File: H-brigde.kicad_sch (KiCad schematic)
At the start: 17 parts, among them J1 track out, J2 track out, U1 L298N

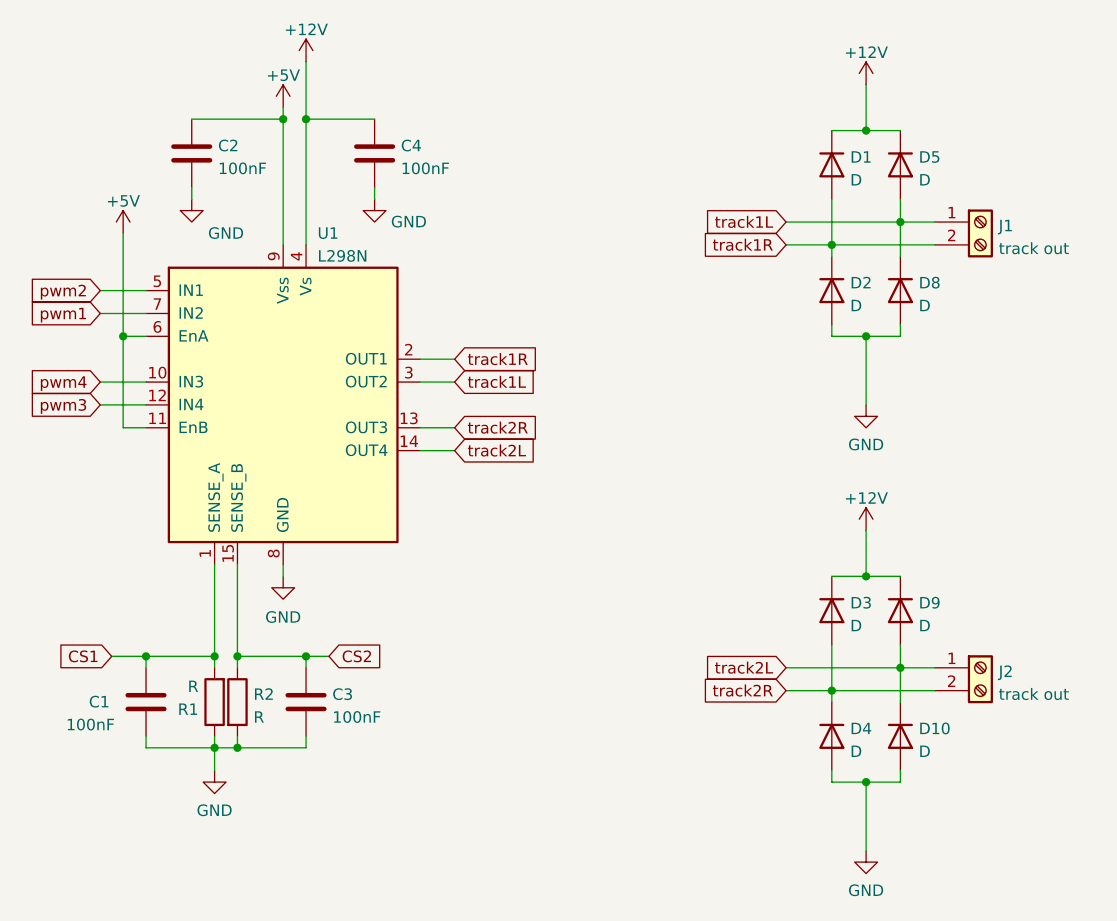
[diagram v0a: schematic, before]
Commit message: redone the switch connectors to accomodate a current sense print. Rearranged parts and updated silk texts to be 50% of their original size
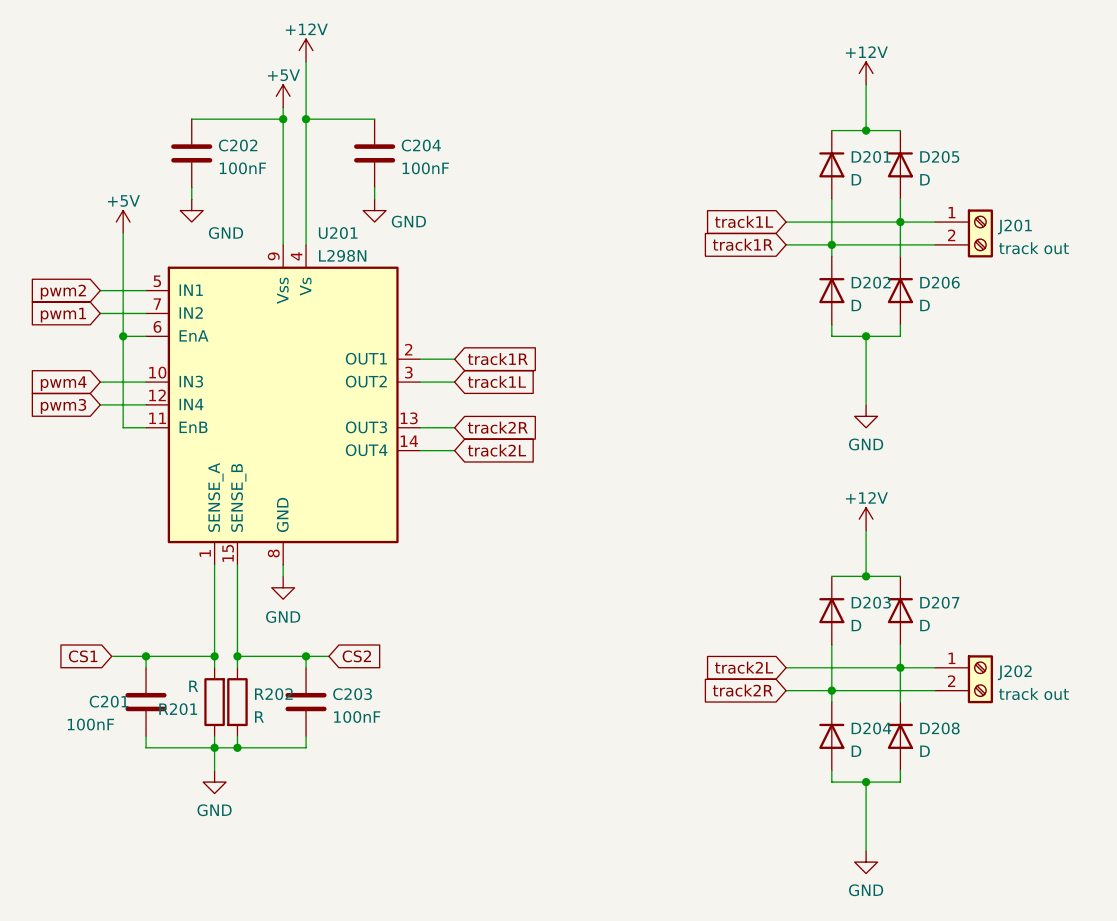
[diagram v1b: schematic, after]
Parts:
- renumbered C1 to C201, C2 to C202, C3 to C203, C4 to C204, D1 to D201, D2 to D202, D3 to D203, D4 to D204, D5 to D205, D8 to D206, D9 to D207, D10 to D208, J1 to J201, J2 to J202, R1 to R201, R2 to R202, U1 to U201
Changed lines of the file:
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@@
   (symbol (lib_id "Device:R") (at 115.57 129.54 180) (unit 1)
     (in_bom yes) (on_board yes) (fields_autoplaced)
-    (property "Reference" "R1" (id 0) (at 113.792 130.3747 0)
+    (property "Reference" "R201" (id 0) (at 113.792 130.3747 0)
       (effects (font (size 1.27 1.27)) (justify left))
     )
@@
   (symbol (lib_id "Device:C") (at 113.03 68.58 0) (unit 1)
     (in_bom yes) (on_board yes) (fields_autoplaced)
-    (property "Reference" "C2" (id 0) (at 115.951 67.7453 0)
+    (property "Reference" "C202" (id 0) (at 115.951 67.7453 0)
       (effects (font (size 1.27 1.27)) (justify left))
     )
@@
   (symbol (lib_id "Device:D") (at 184.15 83.82 270) (unit 1)
     (in_bom yes) (on_board yes) (fields_autoplaced)
-    (property "Reference" "D2" (id 0) (at 186.182 82.9853 90)
+    (property "Reference" "D202" (id 0) (at 186.182 82.9853 90)
       (effects (font (size 1.27 1.27)) (justify left))
     )
@@
   (symbol (lib_id "power:+5V") (at 123.19 63.5 0) (unit 1)
     (in_bom yes) (on_board yes) (fields_autoplaced)
-    (property "Reference" "#PWR0106" (id 0) (at 123.19 67.31 0)
+    (property "Reference" "#PWR0204" (id 0) (at 123.19 67.31 0)
       (effects (font (size 1.27 1.27)) hide)
     )
@@
   (symbol (lib_id "power:+12V") (at 187.96 110.49 0) (unit 1)
     (in_bom yes) (on_board yes) (fields_autoplaced)
-    (property "Reference" "#PWR0103" (id 0) (at 187.96 114.3 0)
+    (property "Reference" "#PWR0210" (id 0) (at 187.96 114.3 0)
       (effects (font (size 1.27 1.27)) hide)
     )
@@
   (symbol (lib_id "power:GND") (at 115.57 137.16 0) (unit 1)
     (in_bom yes) (on_board yes) (fields_autoplaced)
-    (property "Reference" "#PWR0114" (id 0) (at 115.57 143.51 0)
+    (property "Reference" "#PWR0203" (id 0) (at 115.57 143.51 0)
       (effects (font (size 1.27 1.27)) hide)
     )
@@
   (symbol (lib_id "power:GND") (at 187.96 96.52 0) (unit 1)
     (in_bom yes) (on_board yes) (fields_autoplaced)
-    (property "Reference" "#PWR0102" (id 0) (at 187.96 102.87 0)
+    (property "Reference" "#PWR0209" (id 0) (at 187.96 102.87 0)
       (effects (font (size 1.27 1.27)) hide)
     )
@@
   (symbol (lib_id "Device:D") (at 191.77 83.82 270) (unit 1)
     (in_bom yes) (on_board yes) (fields_autoplaced)
-    (property "Reference" "D8" (id 0) (at 193.802 82.9853 90)
+    (property "Reference" "D206" (id 0) (at 193.802 82.9853 90)
       (effects (font (size 1.27 1.27)) (justify left))
     )
@@
   (symbol (lib_id "power:+5V") (at 105.41 77.47 0) (unit 1)
     (in_bom yes) (on_board yes) (fields_autoplaced)
-    (property "Reference" "#PWR0104" (id 0) (at 105.41 81.28 0)
+    (property "Reference" "#PWR0201" (id 0) (at 105.41 81.28 0)
       (effects (font (size 1.27 1.27)) hide)
     )
@@
   (symbol (lib_id "power:GND") (at 133.35 73.66 0) (unit 1)
     (in_bom yes) (on_board yes)
-    (property "Reference" "#PWR0111" (id 0) (at 133.35 80.01 0)
+    (property "Reference" "#PWR0207" (id 0) (at 133.35 80.01 0)
       (effects (font (size 1.27 1.27)) hide)
     )
@@
   (symbol (lib_id "Device:D") (at 184.15 119.38 270) (unit 1)
     (in_bom yes) (on_board yes) (fields_autoplaced)
-    (property "Reference" "D3" (id 0) (at 186.182 118.5453 90)
+    (property "Reference" "D203" (id 0) (at 186.182 118.5453 90)
       (effects (font (size 1.27 1.27)) (justify left))
     )
@@
   (symbol (lib_id "power:+12V") (at 125.73 58.42 0) (unit 1)
     (in_bom yes) (on_board yes) (fields_autoplaced)
-    (property "Reference" "#PWR0110" (id 0) (at 125.73 62.23 0)
+    (property "Reference" "#PWR0206" (id 0) (at 125.73 62.23 0)
       (effects (font (size 1.27 1.27)) hide)
     )
@@
   (symbol (lib_id "Driver_Motor:L298N") (at 123.19 96.52 0) (unit 1)
     (in_bom yes) (on_board yes)
-    (property "Reference" "U1" (id 0) (at 127 77.47 0)
+    (property "Reference" "U201" (id 0) (at 127 77.47 0)
       (effects (font (size 1.27 1.27)) (justify left))
     )
@@
   (symbol (lib_id "Device:C") (at 107.95 129.54 180) (unit 1)
     (in_bom yes) (on_board yes)
-    (property "Reference" "C1" (id 0) (at 101.6 129.54 0)
+    (property "Reference" "C201" (id 0) (at 101.6 129.54 0)
       (effects (font (size 1.27 1.27)) (justify right))
     )
@@
   (symbol (lib_id "power:+12V") (at 187.96 60.96 0) (unit 1)
     (in_bom yes) (on_board yes) (fields_autoplaced)
-    (property "Reference" "#PWR0113" (id 0) (at 187.96 64.77 0)
+    (property "Reference" "#PWR0208" (id 0) (at 187.96 64.77 0)
       (effects (font (size 1.27 1.27)) hide)
     )
@@
   (symbol (lib_id "Device:R") (at 118.11 129.54 0) (unit 1)
     (in_bom yes) (on_board yes) (fields_autoplaced)
-    (property "Reference" "R2" (id 0) (at 119.888 128.7053 0)
+    (property "Reference" "R202" (id 0) (at 119.888 128.7053 0)
       (effects (font (size 1.27 1.27)) (justify left))
     )
@@
   (symbol (lib_id "power:GND") (at 123.19 115.57 0) (unit 1)
     (in_bom yes) (on_board yes) (fields_autoplaced)
-    (property "Reference" "#PWR0112" (id 0) (at 123.19 121.92 0)
+    (property "Reference" "#PWR0205" (id 0) (at 123.19 121.92 0)
       (effects (font (size 1.27 1.27)) hide)
     )
@@
   (symbol (lib_id "power:GND") (at 187.96 146.05 0) (unit 1)
     (in_bom yes) (on_board yes) (fields_autoplaced)
-    (property "Reference" "#PWR0101" (id 0) (at 187.96 152.4 0)
+    (property "Reference" "#PWR0211" (id 0) (at 187.96 152.4 0)
       (effects (font (size 1.27 1.27)) hide)
     )
@@
   (symbol (lib_id "Connector:Screw_Terminal_01x02") (at 200.66 125.73 0) (unit 1)
     (in_bom yes) (on_board yes) (fields_autoplaced)
-    (property "Reference" "J2" (id 0) (at 202.692 126.1653 0)
+    (property "Reference" "J202" (id 0) (at 202.692 126.1653 0)
       (effects (font (size 1.27 1.27)) (justify left))
     )
@@
   (symbol (lib_id "Device:D") (at 191.77 119.38 270) (unit 1)
     (in_bom yes) (on_board yes) (fields_autoplaced)
-    (property "Reference" "D9" (id 0) (at 193.802 118.5453 90)
+    (property "Reference" "D207" (id 0) (at 193.802 118.5453 90)
       (effects (font (size 1.27 1.27)) (justify left))
     )
@@
   (symbol (lib_id "Device:D") (at 191.77 69.85 270) (unit 1)
     (in_bom yes) (on_board yes) (fields_autoplaced)
-    (property "Reference" "D5" (id 0) (at 193.802 69.0153 90)
+    (property "Reference" "D205" (id 0) (at 193.802 69.0153 90)
       (effects (font (size 1.27 1.27)) (justify left))
     )
@@
   (symbol (lib_id "power:GND") (at 113.03 73.66 0) (unit 1)
     (in_bom yes) (on_board yes)
-    (property "Reference" "#PWR0105" (id 0) (at 113.03 80.01 0)
+    (property "Reference" "#PWR0202" (id 0) (at 113.03 80.01 0)
       (effects (font (size 1.27 1.27)) hide)
     )
@@
   (symbol (lib_id "Device:C") (at 133.35 68.58 0) (unit 1)
     (in_bom yes) (on_board yes) (fields_autoplaced)
-    (property "Reference" "C4" (id 0) (at 136.271 67.7453 0)
+    (property "Reference" "C204" (id 0) (at 136.271 67.7453 0)
       (effects (font (size 1.27 1.27)) (justify left))
     )
@@
   (symbol (lib_id "Device:D") (at 184.15 133.35 270) (unit 1)
     (in_bom yes) (on_board yes) (fields_autoplaced)
-    (property "Reference" "D4" (id 0) (at 186.182 132.5153 90)
+    (property "Reference" "D204" (id 0) (at 186.182 132.5153 90)
       (effects (font (size 1.27 1.27)) (justify left))
     )
@@
   (symbol (lib_id "Connector:Screw_Terminal_01x02") (at 200.66 76.2 0) (unit 1)
     (in_bom yes) (on_board yes) (fields_autoplaced)
-    (property "Reference" "J1" (id 0) (at 202.692 76.6353 0)
+    (property "Reference" "J201" (id 0) (at 202.692 76.6353 0)
       (effects (font (size 1.27 1.27)) (justify left))
     )
@@
   (symbol (lib_id "Device:D") (at 191.77 133.35 270) (unit 1)
     (in_bom yes) (on_board yes) (fields_autoplaced)
-    (property "Reference" "D10" (id 0) (at 193.802 132.5153 90)
+    (property "Reference" "D208" (id 0) (at 193.802 132.5153 90)
       (effects (font (size 1.27 1.27)) (justify left))
     )
@@
   (symbol (lib_id "Device:C") (at 125.73 129.54 0) (unit 1)
     (in_bom yes) (on_board yes) (fields_autoplaced)
-    (property "Reference" "C3" (id 0) (at 128.651 128.7053 0)
+    (property "Reference" "C203" (id 0) (at 128.651 128.7053 0)
       (effects (font (size 1.27 1.27)) (justify left))
     )
@@
   (symbol (lib_id "Device:D") (at 184.15 69.85 270) (unit 1)
     (in_bom yes) (on_board yes) (fields_autoplaced)
-    (property "Reference" "D1" (id 0) (at 186.182 69.0153 90)
-      (effects (font (size 1.27 1.27)) (justify left))
-    )
+    (property "Reference" "D201" (id 0) (at 186.182 69.0153 90)
+      (effects (font (size 1.27 1.27)) (justify left))
+    )

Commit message: added something to debug the channel buttons
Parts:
- C201, C202, C203, C204: footprint Capacitor_THT:C_Disc_D3.0mm_W1.6mm_P2.50mm -> Capacitor_SMD:C_0805_2012Metric
- D201, D202, D203, D204, D205, D206, D207, D208: footprint Diode_THT:D_DO-34_SOD68_P7.62mm_Horizontal -> Diode_SMD:D_1206_3216Metric
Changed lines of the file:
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@@
       (effects (font (size 1.27 1.27)) (justify left))
     )
-    (property "Footprint" "Capacitor_THT:C_Disc_D3.0mm_W1.6mm_P2.50mm" (id 2) (at 113.9952 72.39 0)
+    (property "Footprint" "Capacitor_SMD:C_0805_2012Metric" (id 2) (at 113.9952 72.39 0)
       (effects (font (size 1.27 1.27)) hide)
     )
@@
       (effects (font (size 1.27 1.27)) (justify left))
     )
-    (property "Footprint" "Diode_THT:D_DO-34_SOD68_P7.62mm_Horizontal" (id 2) (at 184.15 83.82 0)
+    (property "Footprint" "Diode_SMD:D_1206_3216Metric" (id 2) (at 184.15 83.82 0)
       (effects (font (size 1.27 1.27)) hide)
     )
@@
       (effects (font (size 1.27 1.27)) (justify left))
     )
-    (property "Footprint" "Diode_THT:D_DO-34_SOD68_P7.62mm_Horizontal" (id 2) (at 191.77 83.82 0)
+    (property "Footprint" "Diode_SMD:D_1206_3216Metric" (id 2) (at 191.77 83.82 0)
       (effects (font (size 1.27 1.27)) hide)
     )
@@
       (effects (font (size 1.27 1.27)) (justify left))
     )
-    (property "Footprint" "Diode_THT:D_DO-34_SOD68_P7.62mm_Horizontal" (id 2) (at 184.15 119.38 0)
+    (property "Footprint" "Diode_SMD:D_1206_3216Metric" (id 2) (at 184.15 119.38 0)
       (effects (font (size 1.27 1.27)) hide)
     )
@@
       (effects (font (size 1.27 1.27)) (justify right))
     )
-    (property "Footprint" "Capacitor_THT:C_Disc_D3.0mm_W1.6mm_P2.50mm" (id 2) (at 106.9848 125.73 0)
+    (property "Footprint" "Capacitor_SMD:C_0805_2012Metric" (id 2) (at 106.9848 125.73 0)
       (effects (font (size 1.27 1.27)) hide)
     )
@@
       (effects (font (size 1.27 1.27)) (justify left))
     )
-    (property "Footprint" "Diode_THT:D_DO-34_SOD68_P7.62mm_Horizontal" (id 2) (at 191.77 119.38 0)
+    (property "Footprint" "Diode_SMD:D_1206_3216Metric" (id 2) (at 191.77 119.38 0)
       (effects (font (size 1.27 1.27)) hide)
     )
@@
       (effects (font (size 1.27 1.27)) (justify left))
     )
-    (property "Footprint" "Diode_THT:D_DO-34_SOD68_P7.62mm_Horizontal" (id 2) (at 191.77 69.85 0)
+    (property "Footprint" "Diode_SMD:D_1206_3216Metric" (id 2) (at 191.77 69.85 0)
       (effects (font (size 1.27 1.27)) hide)
     )
@@
       (effects (font (size 1.27 1.27)) (justify left))
     )
-    (property "Footprint" "Capacitor_THT:C_Disc_D3.0mm_W1.6mm_P2.50mm" (id 2) (at 134.3152 72.39 0)
+    (property "Footprint" "Capacitor_SMD:C_0805_2012Metric" (id 2) (at 134.3152 72.39 0)
       (effects (font (size 1.27 1.27)) hide)
     )
@@
       (effects (font (size 1.27 1.27)) (justify left))
     )
-    (property "Footprint" "Diode_THT:D_DO-34_SOD68_P7.62mm_Horizontal" (id 2) (at 184.15 133.35 0)
+    (property "Footprint" "Diode_SMD:D_1206_3216Metric" (id 2) (at 184.15 133.35 0)
       (effects (font (size 1.27 1.27)) hide)
     )
@@
       (effects (font (size 1.27 1.27)) (justify left))
     )
-    (property "Footprint" "Diode_THT:D_DO-34_SOD68_P7.62mm_Horizontal" (id 2) (at 191.77 133.35 0)
+    (property "Footprint" "Diode_SMD:D_1206_3216Metric" (id 2) (at 191.77 133.35 0)
       (effects (font (size 1.27 1.27)) hide)
     )
@@
       (effects (font (size 1.27 1.27)) (justify left))
     )
-    (property "Footprint" "Capacitor_THT:C_Disc_D3.0mm_W1.6mm_P2.50mm" (id 2) (at 126.6952 133.35 0)
+    (property "Footprint" "Capacitor_SMD:C_0805_2012Metric" (id 2) (at 126.6952 133.35 0)
       (effects (font (size 1.27 1.27)) hide)
     )
@@
       (effects (font (size 1.27 1.27)) (justify left))
     )
-    (property "Footprint" "Diode_THT:D_DO-34_SOD68_P7.62mm_Horizontal" (id 2) (at 184.15 69.85 0)
-      (effects (font (size 1.27 1.27)) hide)
-    )
+    (property "Footprint" "Diode_SMD:D_1206_3216Metric" (id 2) (at 184.15 69.85 0)
+      (effects (font (size 1.27 1.27)) hide)
+    )

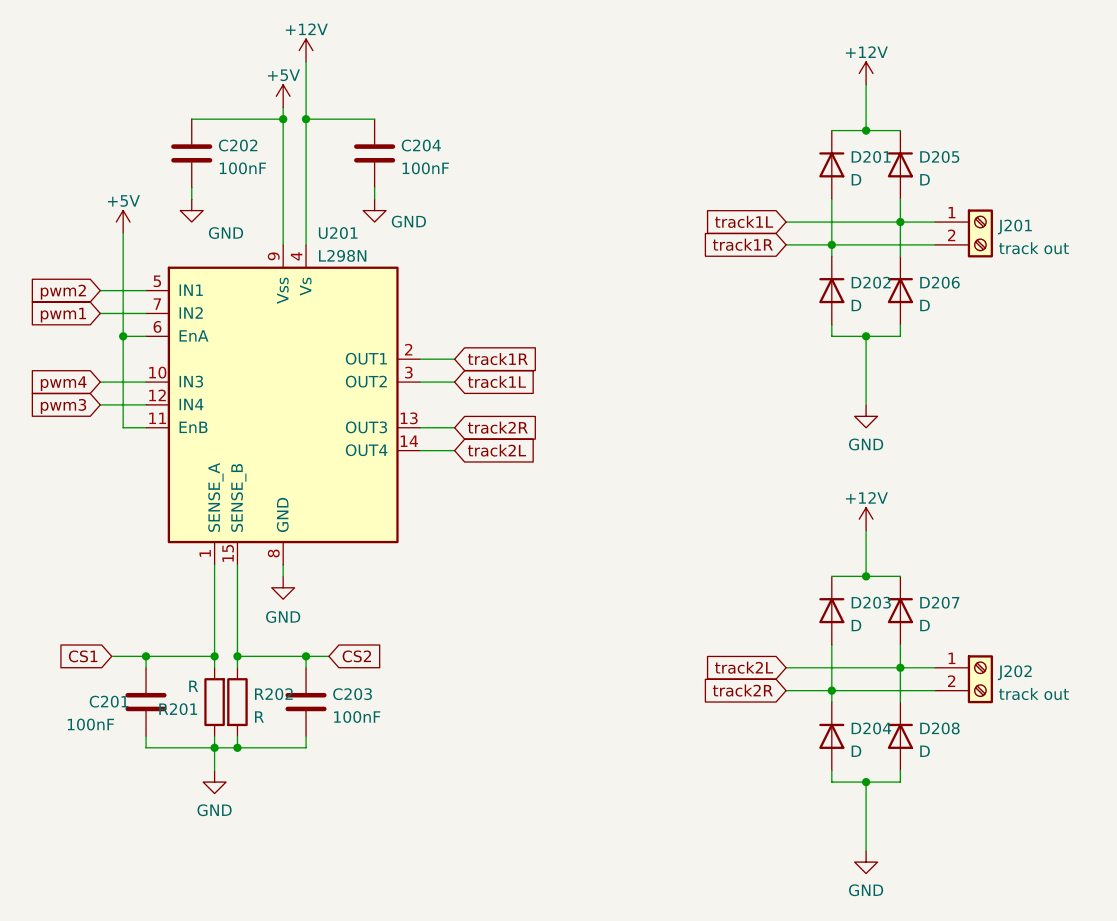
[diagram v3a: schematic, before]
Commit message: redid this project. I want to use an atmega328 so I ditched some IO. I retained 4 servo, 1 H-bridge (should make it double), 3 relays, 6 GPIO, 1 potentiometer and loconet interface. And I still have a config button
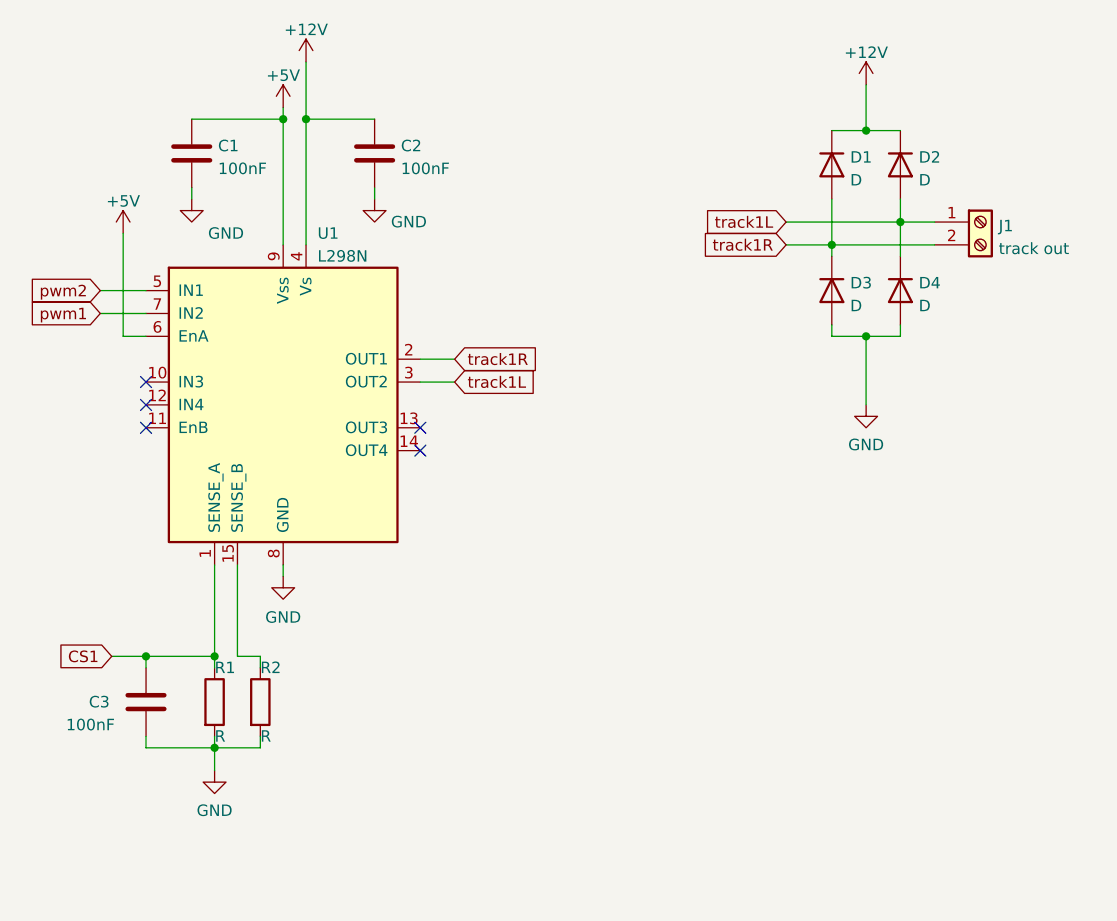
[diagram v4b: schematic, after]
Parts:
- removed C203: 100nF, Capacitor_SMD:C_0805_2012Metric, symbol Device:C
- removed D203, D204, D207, D208: D, Diode_SMD:D_1206_3216Metric, symbol Device:D
- removed J202: track out, TerminalBlock_Phoenix:TerminalBlock_Phoenix_MKDS-1,5-2-5.08_1x02_P5.08mm_Horizontal, symbol Connector:Screw_Terminal_01x02
- removed R201, R202: R, Resistor_THT:R_Axial_DIN0516_L15.5mm_D5.0mm_P20.32mm_Horizontal, symbol Device:R
- added R1, R2: R, Resistor_SMD:R_1206_3216Metric_Pad1.30x1.75mm_HandSolder, symbol Device:R
- renumbered C202 to C1, C204 to C2, C201 to C3, D201 to D1, D205 to D2, D202 to D3, D206 to D4, J201 to J1, U201 to U1
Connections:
- net +5V: no longer U1.11 (EnB)
- net CS1: now also R1.1
- net GND: now also R1.2, R2.2
- net CS2: no longer names the net of U1.15 (SENSE_B)
- net CS2: now also R2.1
- net pwm3: no longer names the net of U1.12 (IN4)
- net pwm4: no longer names the net of U1.10 (IN3)
- net track2L: no longer names the net of U1.14 (OUT4)
- net track2R: no longer names the net of U1.13 (OUT3)
- no-connect marks 0 -> 5
